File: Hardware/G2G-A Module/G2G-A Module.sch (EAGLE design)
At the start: 4 parts, among them J1 GROVE-4P-2.0-3470130P1

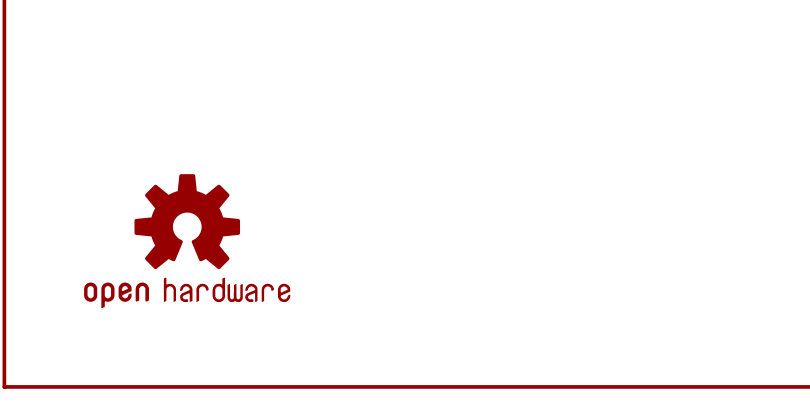
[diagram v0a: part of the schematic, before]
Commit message: Replaced all 'G' logos with a new part for the logo.
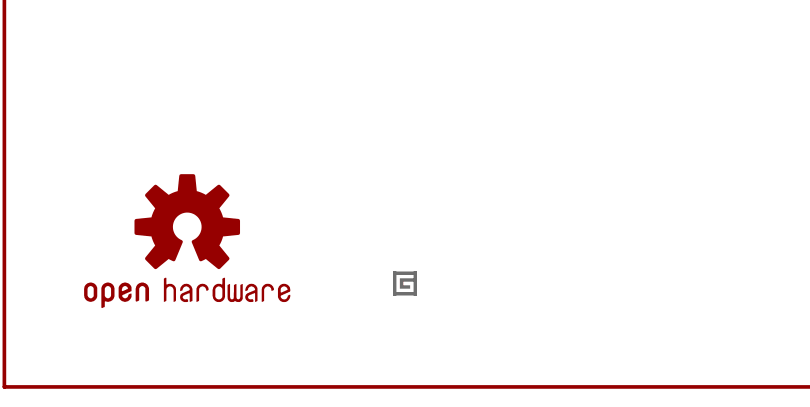
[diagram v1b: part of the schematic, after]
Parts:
- added U$2: GADGETEER_LOGO_SMALL, SoftDust:GADGETEER_LOGO_SMALL
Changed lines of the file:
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@@
 <attribute name="VERSION" value="v1.0"/>
 </part>
+<part name="U$2" library="SoftDust" deviceset="GADGETEER_LOGO_SMALL" device=""/>
 </parts>
 <sheets>
@@
 <instance part="FRAME1" gate="G$1" x="0" y="0"/>
 <instance part="FRAME1" gate="V" x="147.32" y="0"/>
+<instance part="U$2" gate="G$1" x="43.18" y="10.16"/>
 </instances>
 <busses>
